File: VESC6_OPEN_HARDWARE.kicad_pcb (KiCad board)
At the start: 2 copper layers, 80 x 78 mm, 117 parts, among them P1 USB_OTG, P2 TS_CAN, P3 SWD, P4 HALL/Encoder, P7 Custom, Q1 STL130N6F7, Q2 STL130N6F7, Q3 STL130N6F7, Q4 STL130N6F7, Q5 STL130N6F7, Q6 STL130N6F7, U1 STM32F40X_LQFP64, U10 LSM6DS3TR-C, U2 LM3671, U3 DRV8301, U4 TJA1051TK-3, U5 AD8418, U6 AD8418, U7 AD8418, X1 8m

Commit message: started power stage
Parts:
- removed TP1, TP2: TestPoint, TestPoint:TestPoint_Pad_D1.5mm
- added P10: PH_A, Connector_Pin:Pin_D1.0mm_L10.0mm_LooseFit, F.Cu at (32.5, 62.8)
- added P11: SUPPLY, Connector_Pin:Pin_D1.0mm_L10.0mm_LooseFit, F.Cu at (186.5, 62.0)
- added P12: GND, Connector_Pin:Pin_D1.0mm_L10.0mm_LooseFit, F.Cu at (186.5, 48.0)
- added P8: PH_C, Connector_Pin:Pin_D1.0mm_L10.0mm_LooseFit, F.Cu at (31.5, 32.5)
- added P9: PH_B, Connector_Pin:Pin_D1.0mm_L10.0mm_LooseFit, F.Cu at (31.6, 46.8)
- moved X1 230.4 mm to (286.6, -39.7)
- moved C2 230.1 mm to (291.3, -37.7)
- moved C8 228.8 mm to (291.4, -40.7)
- moved C3 210.3 mm to (256.4, -45.3)
- moved C4 210.3 mm to (256.4, -42.8)
- moved C5 210.3 mm to (256.4, -40.3)
- moved C6 210.3 mm to (256.4, -37.7)
- moved C7 210.3 mm to (256.4, -35.2)
- moved C33 186.5 mm to (243.8, -40.1)
- moved C34 186.5 mm to (243.8, -37.6)
- moved R23 186.5 mm to (243.8, -35.0)
- moved U4 185.2 mm to (247.8, -38.1)
- moved P2 175.3 mm to (243.8, -43.9), turned to 90 degrees
- moved C64 172.1 mm to (267.7, -38.7)
- moved L1 167.8 mm to (271.9, -34.2)
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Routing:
- net Net-(P8-Pin_1): track 0.00 -> 30.6 mm, vias 0 -> 1
- net /DRV8301/SH_C: track 0.00 -> 29.2 mm, vias 0 -> 1
- net /DRV8301/GL_C: track 0.00 -> 27.4 mm, vias 0 -> 1
- net /DRV8301/GH_C: track 0.00 -> 18.9 mm, vias 0 -> 1
- net Net-(P9-Pin_1): track 0.00 -> 9.09 mm, vias 0 -> 1
- net /DRV8301/SH_B: track 0.00 -> 6.41 mm, vias 0 -> 1
- net Net-(Q2-G): track 0.00 -> 2.36 mm
- net Net-(Q1-G): track 0.00 -> 2.08 mm
- net /power/CURR_C: track 0.00 -> 1.61 mm
- net Net-(Q3-G): track 0.00 -> 1.35 mm, vias 0 -> 1
- net /DRV8301/SENS_C: track 0.00 -> 1.35 mm
- net Net-(Q4-G): track 0.00 -> 1.25 mm, vias 0 -> 1
- net GND: vias 0 -> 10
- added copper zone on F.Cu, net /DRV8301/SH_B
- added copper zone on F.Cu, net /DRV8301/SH_C
- added copper zone on F.Cu, net GND
- added copper zone on F.Cu, net SUPPLY
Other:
- board size 80 x 78 mm -> 248 x 62 mm

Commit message: power stage complete
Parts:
- moved C36 52.1 mm to (50.3, 69.0)
- moved R28 52.1 mm to (50.3, 70.5)
- moved R27 48.2 mm to (52.6, 69.8), turned to 90 degrees
- moved R35 17.6 mm to (67.3, 57.7)
- moved R22 16.2 mm to (74.9, 43.3), turned to 180 degrees
- moved R36 14.7 mm to (67.2, 47.8)
- moved C29 14.4 mm to (67.3, 59.2), turned to 0 degrees
- moved R21 13.5 mm to (71.9, 43.3), turned to 0 degrees
- moved C39 13.4 mm to (67.6, 41.7)
- moved Q1 13.4 mm to (61.4, 43.4)
- moved R26 13.4 mm to (49.0, 38.2)
- moved Q2 13.4 mm to (54.0, 41.3)
- moved C37 13.4 mm to (67.6, 45.0)
- moved R24 13.4 mm to (46.6, 42.3)
- moved P8 13.0 mm to (40.2, 42.2)
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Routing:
- net Net-(Q3-G): track 1.35 -> 48.6 mm
- net /DRV8301/GH_A: track 0.00 -> 40.8 mm, vias 0 -> 1
- net Net-(P10-Pin_1): track 0.00 -> 37.1 mm, vias 0 -> 2
- net /DRV8301/GL_B: track 0.00 -> 36.6 mm, vias 0 -> 1
- net /DRV8301/GL_A: track 0.00 -> 36.5 mm, vias 0 -> 1
- net /DRV8301/SH_A: track 0.00 -> 36.5 mm, vias 0 -> 2
- net /DRV8301/SH_B: track 6.41 -> 37.3 mm, vias 1 -> 2
- net Net-(P9-Pin_1): track 9.09 -> 37.5 mm, vias 1 -> 2
- net /DRV8301/GH_C: track 18.9 -> 39.5 mm
- net GND: track 0.00 -> 12.5 mm, vias 10 -> 27
- net VCC: track 0.00 -> 10.1 mm
- net Net-(Q5-G): track 0.00 -> 8.78 mm
- net /DRV8301/GL_C: track 27.4 -> 35.6 mm
- net /DRV8301/SH_C: track 29.2 -> 37.0 mm, vias 1 -> 2
- net Net-(Q1-G): track 2.08 -> 9.07 mm
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- added copper zone on F.Cu, net /DRV8301/SH_A
- removed copper zone on F.Cu, net GND
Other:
- outline, holes or cut-outs redrawn
- board text added: "FET TEMP"
- board text added: "PHASE A"
- board text added: "PHASE B"
- board text added: "PHASE C"
- board text added: "POWER STAGE"

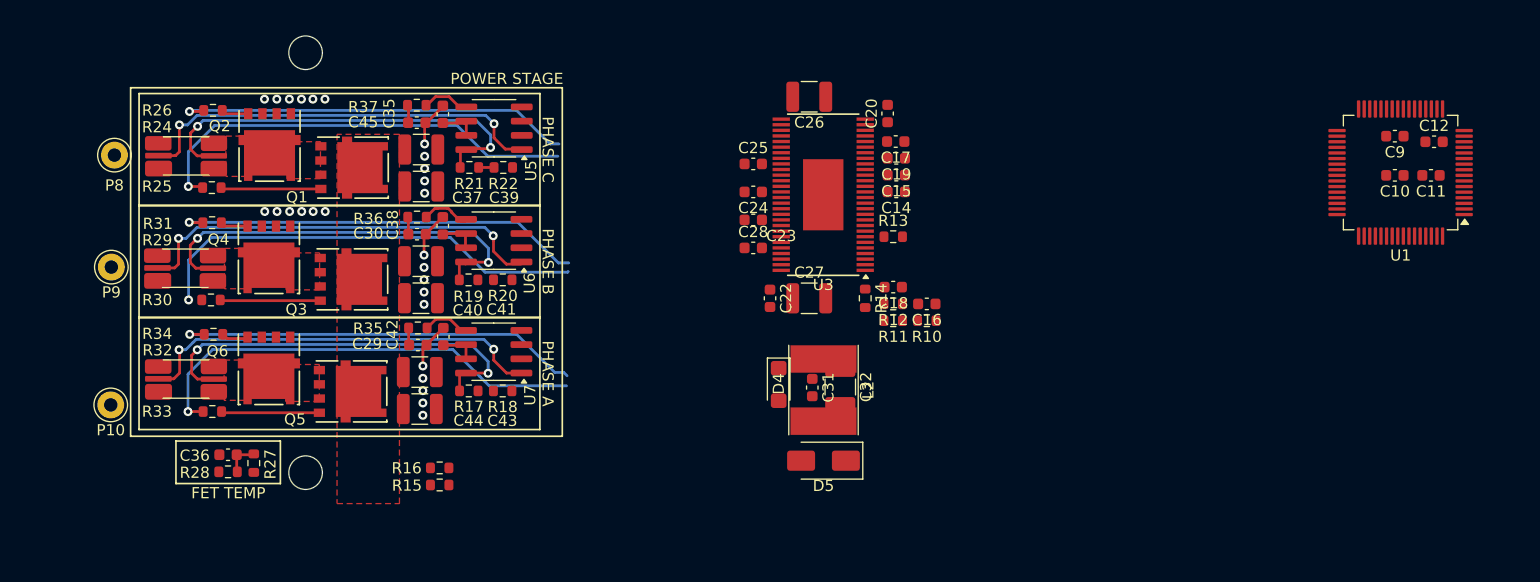
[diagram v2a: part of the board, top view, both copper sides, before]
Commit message: DRV8301 Stage Complete
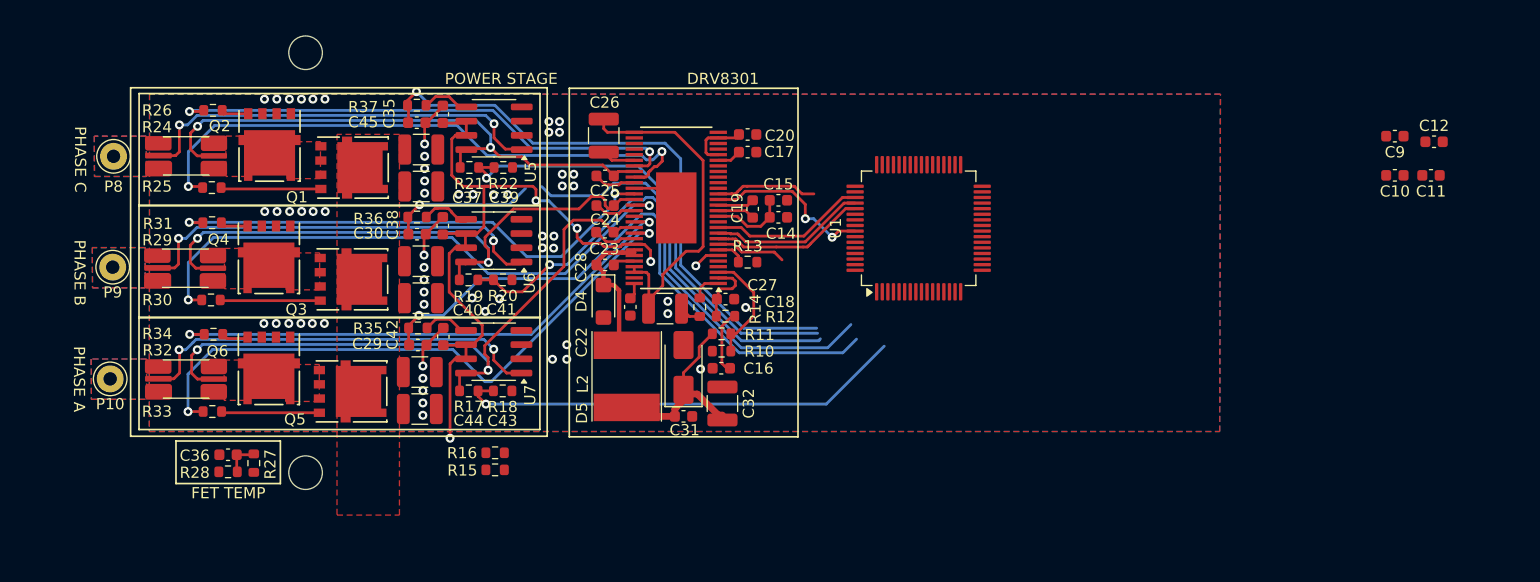
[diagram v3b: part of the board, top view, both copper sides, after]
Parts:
- moved U1 43.3 mm to (112.0, 48.8), turned to 90 degrees
- moved C16 19.2 mm to (94.4, 61.3), turned to 0 degrees
- moved C26 18.7 mm to (83.9, 40.5), turned to -90 degrees
- moved R10 18.5 mm to (94.4, 59.8), turned to 0 degrees
- moved L2 17.6 mm to (85.9, 62.0)
- moved D4 17.3 mm to (83.9, 55.3)
- moved R11 15.4 mm to (94.4, 58.2)
- moved D5 15.0 mm to (91.0, 61.2), turned to 90 degrees
- moved R12 15.0 mm to (94.8, 56.6)
- moved C18 15.0 mm to (94.8, 55.1)
- moved R14 14.8 mm to (92.5, 55.8), turned to 90 degrees
- moved C19 13.6 mm to (97.2, 47.0), turned to 90 degrees
- moved C28 13.3 mm to (84.0, 52.0)
- moved C23 13.3 mm to (84.0, 49.1)
- moved C24 13.3 mm to (84.0, 46.8)
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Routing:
- net VCC: track 10.1 -> 64.1 mm, vias 0 -> 4
- net /power/CURR_A: track 1.55 -> 54.3 mm, vias 0 -> 1
- net /DRV8301/GH_B: track 0.00 -> 52.1 mm, vias 0 -> 2
- net /power/CURR_C: track 1.62 -> 53.2 mm, vias 0 -> 1
- net /DRV8301/SENS_B: track 0.00 -> 46.9 mm, vias 0 -> 1
- net /power/CURR_B: track 1.55 -> 48.0 mm, vias 0 -> 1
- net /DRV8301/SENS_C: track 1.35 -> 42.2 mm, vias 0 -> 1
- net /DRV8301/SENS_A: track 0.00 -> 40.6 mm, vias 0 -> 1
- net Net-(Q3-G): track 48.6 -> 8.96 mm, vias 1 -> 0
- net SUPPLY: track 0.00 -> 30.9 mm
- net /DRV8301/SH_A: track 36.5 -> 59.2 mm
- net /DRV8301/SH_B: track 37.3 -> 55.4 mm
- net +5V: track 0.00 -> 17.8 mm
- net /DRV8301/EN_GATE: track 0.00 -> 15.2 mm, vias 0 -> 2
- net /DRV8301/GH_A: track 40.8 -> 54.9 mm, vias 1 -> 2
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- added copper zone on B.Cu, net GND
- added copper zone on F.Cu, net GND
- added copper zone on B.Cu, net Net-(P10-Pin_1)
- added copper zone on F.Cu, net Net-(P10-Pin_1)
- added copper zone on B.Cu, net Net-(P8-Pin_1)
- added copper zone on F.Cu, net Net-(P8-Pin_1)
- added copper zone on B.Cu, net Net-(P9-Pin_1)
- added copper zone on F.Cu, net Net-(P9-Pin_1)
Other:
- board text added: "DRV8301"

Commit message: Begun wiring main MCU
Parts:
- moved C58 209.9 mm to (36.8, 39.9)
- moved P4 209.9 mm to (40.3, 31.1)
- moved R39 209.9 mm to (36.8, 29.9)
- moved R42 209.9 mm to (36.8, 32.4)
- moved R43 209.9 mm to (36.8, 34.9)
- moved R44 209.9 mm to (36.8, 37.4)
- moved C2 206.0 mm to (111.0, 61.9), turned to 180 degrees
- moved C8 204.7 mm to (114.3, 61.9)
- moved X1 200.1 mm to (112.7, 59.2)
- moved C21 197.1 mm to (104.2, 61.1), turned to 180 degrees
- moved L1 195.9 mm to (102.8, 64.6), turned to 90 degrees
- moved U2 195.4 mm to (105.8, 64.5), turned to 180 degrees
- moved C13 190.6 mm to (109.2, 64.2), turned to 90 degrees
- moved C64 188.9 mm to (107.3, 61.2), turned to 90 degrees
- moved C7 177.2 mm to (105.7, 58.0), turned to -90 degrees
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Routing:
- net VCC: track 64.1 -> 139.4 mm, vias 4 -> 7
- net /DRV8301/SENS_SUPPLY: track 0.00 -> 52.6 mm, vias 0 -> 1
- net /DRV8301/INL_B: track 0.00 -> 27.2 mm, vias 0 -> 2
- net /DRV8301/INL_A: track 0.00 -> 26.2 mm, vias 0 -> 2
- net /DRV8301/INL_C: track 0.00 -> 25.5 mm, vias 0 -> 2
- net /CAN/CANH: track 0.00 -> 24.5 mm, vias 0 -> 1
- net /CAN/CANL: track 0.00 -> 23.0 mm, vias 0 -> 1
- net +5V: track 17.8 -> 39.9 mm, vias 0 -> 1
- net /DRV8301/INH_B: track 0.00 -> 21.4 mm
- net /DRV8301/INH_C: track 0.00 -> 20.2 mm
- net /DRV8301/SENS_C: track 42.2 -> 61.8 mm, vias 1 -> 2
- net /power/CURR_C: track 53.2 -> 71.9 mm, vias 1 -> 2
- net /power/CURR_B: track 48.0 -> 62.9 mm, vias 1 -> 2
- net /DRV8301/SENS_B: track 46.9 -> 61.0 mm, vias 1 -> 2
- net /DRV8301/INH_A: track 9.11 -> 22.2 mm, vias 0 -> 2
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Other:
- board size 248 x 62 mm -> 103.3 x 45.2 mm

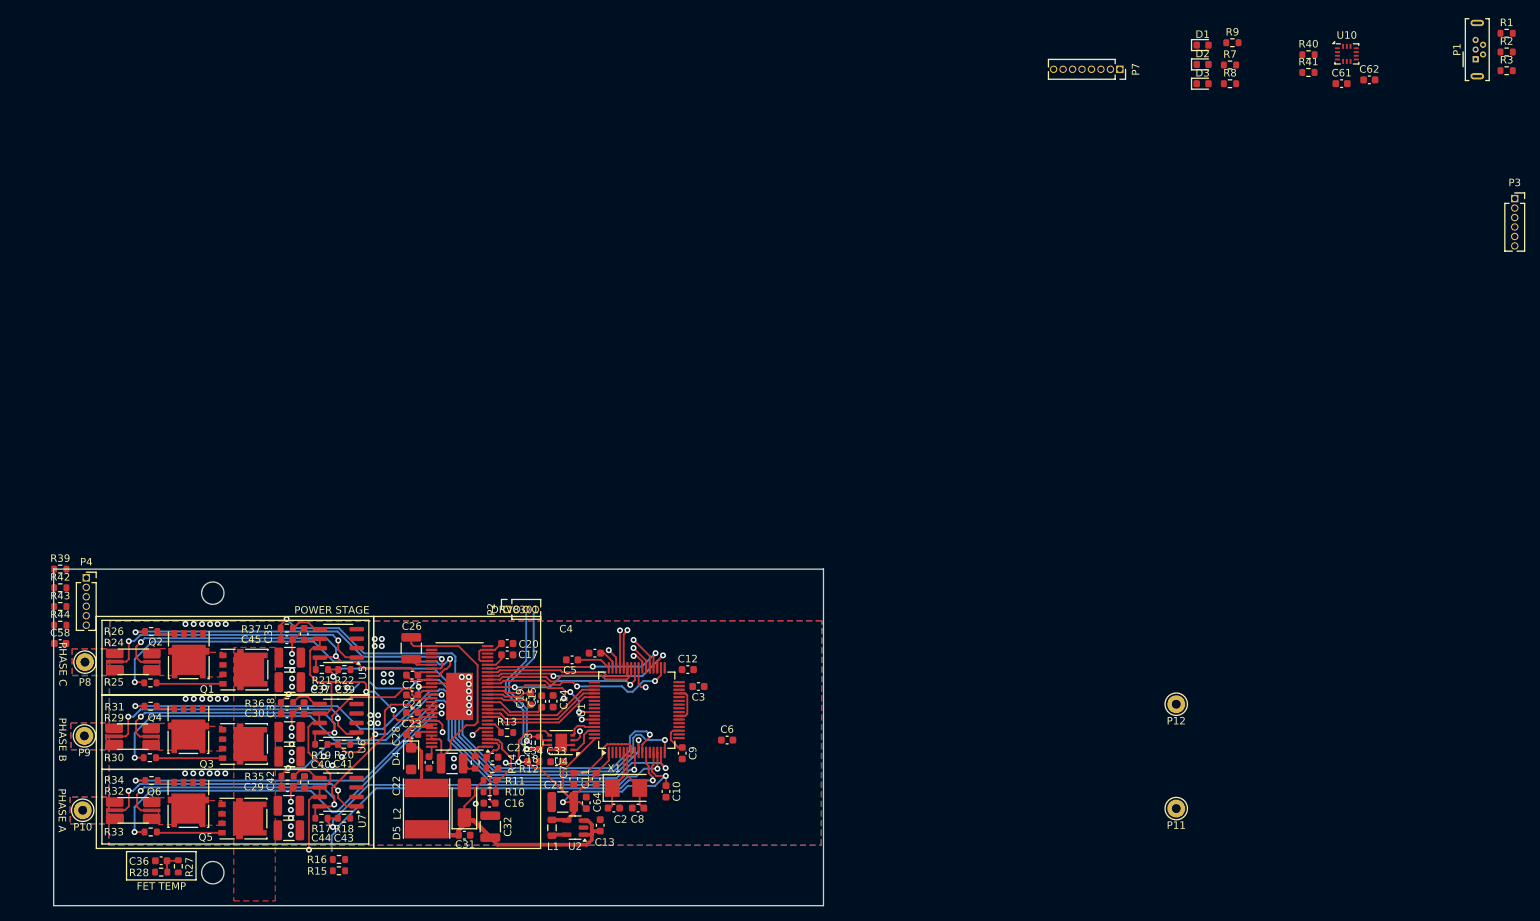
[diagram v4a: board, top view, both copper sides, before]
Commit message: more routing connectors and caps
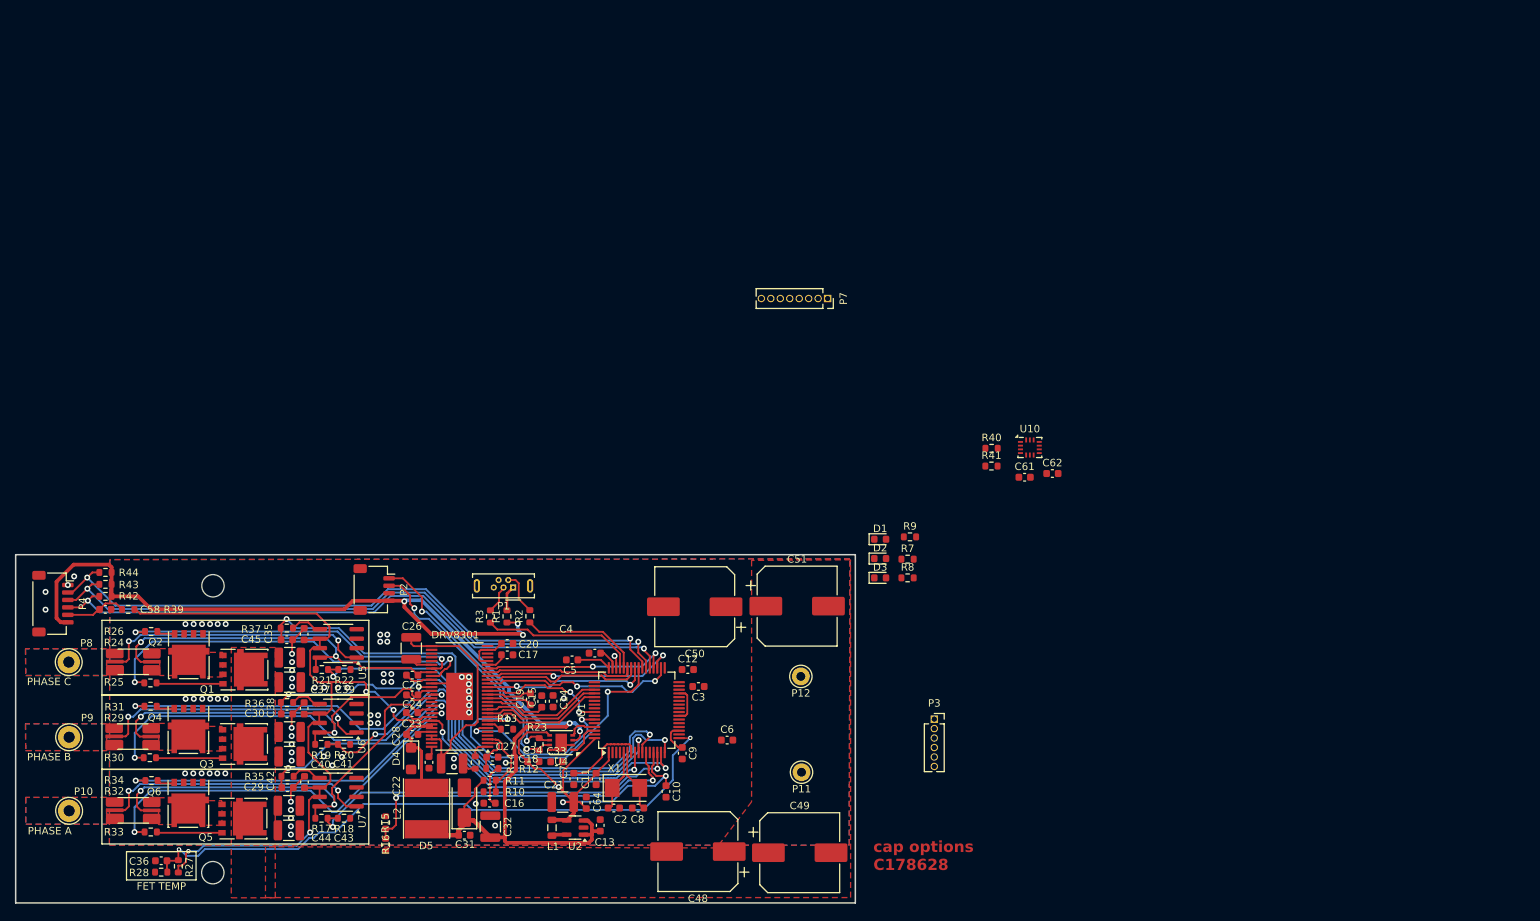
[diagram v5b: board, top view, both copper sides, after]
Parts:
- added C48: 680u_63v, Capacitor_SMD:CP_Elec_10x10.5, F.Cu at (122.3, 67.8)
- added C49: 680u_63v, Capacitor_SMD:CP_Elec_10x10.5, F.Cu at (136.0, 67.9)
- added C50: 680u_63v, Capacitor_SMD:CP_Elec_10x10.5, F.Cu at (121.9, 34.9)
- added C51: 680u_63v, Capacitor_SMD:CP_Elec_10x10.5, F.Cu at (135.6, 34.8)
- P10, P8, P9: footprint Connector_Pin:Pin_D1.0mm_L10.0mm_LooseFit -> Connector_Pin:Pin_D1.3mm_L11.0mm_LooseFit
- P2: footprint Connector_PinSocket_1.27mm:PinSocket_1x04_P1.27mm_Vertical -> Connector_JST:JST_SH_SM04B-SRSS-TB_1x04-1MP_P1.00mm_Horizontal
- P4: footprint Connector_PinSocket_1.27mm:PinSocket_1x06_P1.27mm_Vertical -> Connector_JST:JST_SH_SM06B-SRSS-TB_1x06-1MP_P1.00mm_Horizontal
- moved R1 155.3 mm to (96.7, 36.2), turned to 90 degrees
- moved R3 154.8 mm to (94.5, 36.2), turned to 90 degrees
- moved R2 151.3 mm to (99.8, 36.2), turned to 90 degrees
- moved P1 147.3 mm to (97.5, 32.3), turned to 180 degrees
- moved P3 104.6 mm to (154.0, 50.0)
- moved D1 79.2 mm to (146.8, 25.9)
- moved D2 79.2 mm to (146.8, 28.5)
- moved D3 79.2 mm to (146.8, 31.1)
- moved R7 79.2 mm to (150.5, 28.5)
- moved R8 79.2 mm to (150.5, 31.1)
- moved R9 79.2 mm to (150.8, 25.6)
- moved C61 67.8 mm to (166.2, 17.6)
- moved C62 67.8 mm to (169.9, 17.1)
- moved R40 67.8 mm to (161.7, 13.7)
- moved R41 67.8 mm to (161.7, 16.1)
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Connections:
- P2 pad 1: +5V -> /CAN/CANL
- P2 pad 2: GND -> /CAN/CANH
- P2 pad 3: /CAN/CANH -> GND
- P2 pad 4: /CAN/CANL -> +5V
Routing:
- net +5V: track 39.9 -> 174.7 mm, vias 1 -> 5
- net /stm32f40x/HALL_3: track 2.46 -> 88.2 mm, vias 1 -> 2
- net /stm32f40x/HALL_2: track 3.36 -> 88.0 mm, vias 1 -> 2
- net /stm32f40x/HALL_1: track 4.65 -> 86.9 mm, vias 1 -> 2
- net /power/TEMP: track 3.10 -> 84.2 mm, vias 0 -> 2
- net VCC: track 139.4 -> 206.3 mm, vias 7 -> 8
- net /DRV8301/CS: track 3.33 -> 41.4 mm, vias 1 -> 2
- net /DRV8301/FAULT: track 4.09 -> 22.7 mm
- net /stm32f40x/USB_DP: track 5.02 -> 21.0 mm, vias 1 -> 0
- net /stm32f40x/USB_DM: track 5.27 -> 16.3 mm, vias 1 -> 0
- net /CAN/CANL: track 23.0 -> 33.8 mm, vias 1 -> 2
- net /CAN/CANH: track 24.5 -> 34.1 mm, vias 1 -> 2
- net /stm32f40x/TEMP_MOTOR: track 0.00 -> 8.37 mm
- net /DRV8301/SENS_SUPPLY: track 52.6 -> 46.1 mm, vias 1 -> 2
- net Net-(P1-D-): track 0.00 -> 5.80 mm
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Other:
- board size 103.3 x 45.2 mm -> 112.6 x 46.7 mm
- board text added: "Mounting hole placement SMD electrolytic Cap placement Phase and power connector sizes"
- board text added: "cap options C178628"
- board text removed: "POWER STAGE"
